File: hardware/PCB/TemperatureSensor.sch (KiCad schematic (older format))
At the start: 18 parts, among them IC1 BQ24092DGQR, IC2 ESP32-D0WD-V3, IC3 SHT31-ARP-B2.5kS, J1 USB_B_Micro, U1 LTR-329ALS-01, U2 FT230XQ

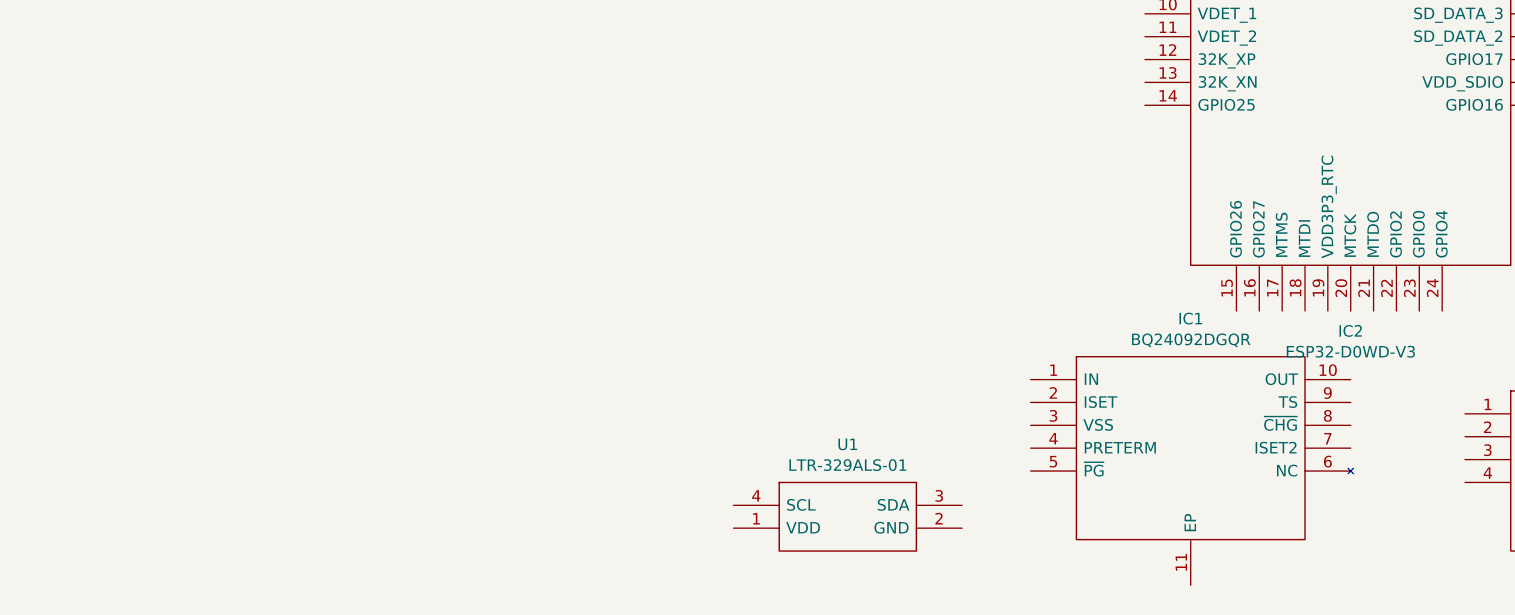
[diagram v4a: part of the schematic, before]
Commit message: Add BQ24092DGQR for LiPo charging
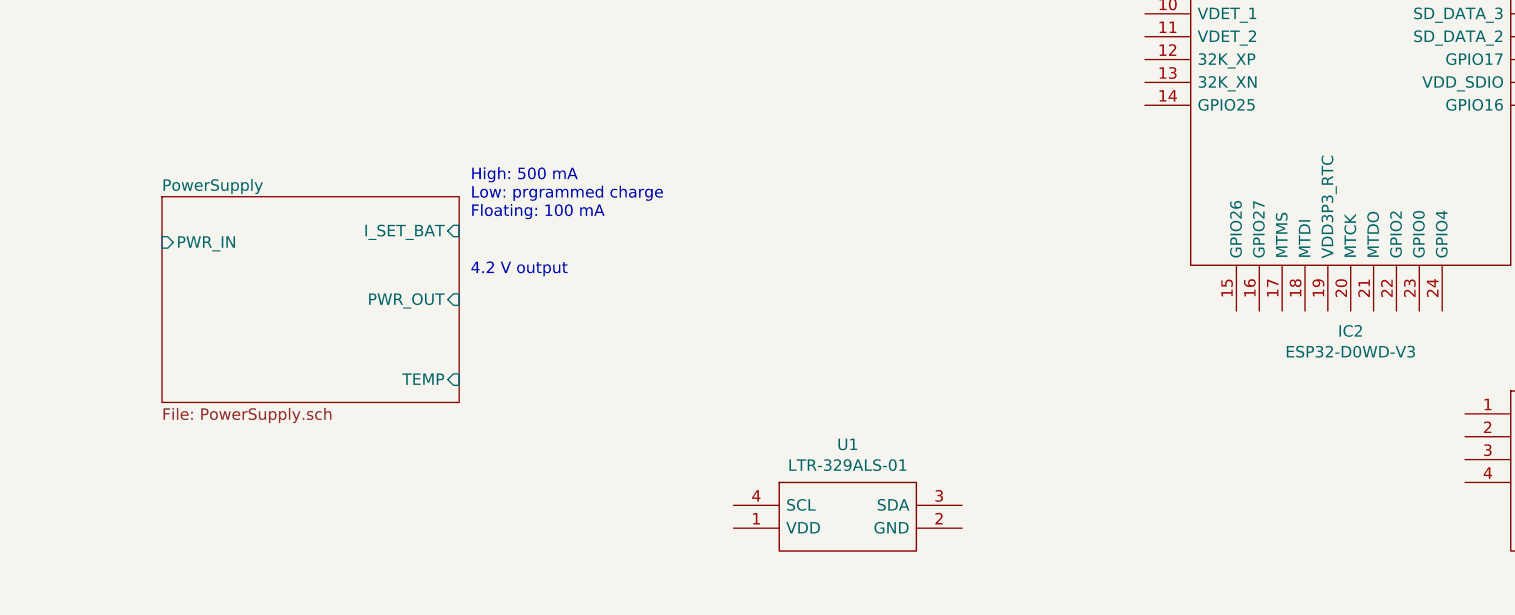
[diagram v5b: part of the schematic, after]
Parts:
- removed IC1: BQ24092DGQR, SOP50P490X110-11N, symbol ProjectLibrary:BQ24092DGQR
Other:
- note added: "4.2 V output"
- note added: "High: 500 mA\nLow: prgrammed charge\nFloating: 100 mA"
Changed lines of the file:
@@
 $Descr A4 11693 8268
 encoding utf-8
-Sheet 1 2
+Sheet 1 3
 Title ""
 Date ""
@@
 Comment4 ""
 $EndDescr
-$Comp
-L ProjectLibrary:BQ24092DGQR IC1
-U 1 1 5FB42655
-P 7900 5500
-F 0 "IC1" H 8600 5765 50  0000 C CNN
-F 1 "BQ24092DGQR" H 8600 5674 50  0000 C CNN
-F 2 "SOP50P490X110-11N" H 9150 5600 50  0001 L CNN
-F 3 "http://www.ti.com/lit/gpn/BQ24092" H 9150 5500 50  0001 L CNN
-F 4 "1A, Single-Input, Single-Cell Li-Ion Battery Charger with Operation Over JEITA and 10k NTC" H 9150 5400 50  0001 L CNN "Description"
-F 5 "1.1" H 9150 5300 50  0001 L CNN "Height"
-F 6 "595-BQ24092DGQR" H 9150 5200 50  0001 L CNN "Mouser Part Number"
-F 7 "https://www.mouser.co.uk/ProductDetail/Texas-Instruments/BQ24092DGQR?qs=C44r%252BX3hXgKGrpCEuObqhg%3D%3D" H 9150 5100 50  0001 L CNN "Mouser Price/Stock"
-F 8 "Texas Instruments" H 9150 5000 50  0001 L CNN "Manufacturer_Name"
-F 9 "BQ24092DGQR" H 9150 4900 50  0001 L CNN "Manufacturer_Part_Number"
-	1    7900 5500
-	1    0    0    -1
-$EndComp
 $Comp
 L ProjectLibrary:ESP32-D0WD-V3 IC2
@@
 Wire Wire Line
 	600  2950 600  3150
+$Sheet
+S 4100 4700 1300 900
+U 5FBFD530
+F0 "PowerSupply" 50
+F1 "PowerSupply.sch" 50
+F2 "PWR_IN" I L 4100 4900 50
+F3 "I_SET_BAT" I R 5400 4850 50
+F4 "TEMP" I R 5400 5500 50
+F5 "PWR_OUT" I R 5400 5150 50
+$EndSheet
+Text Notes 5450 4800 0    50   ~ 0
+High: 500 mA\nLow: prgrammed charge\nFloating: 100 mA
+Text Notes 5450 5050 0    50   ~ 0
+4.2 V output
 $EndSCHEMATC

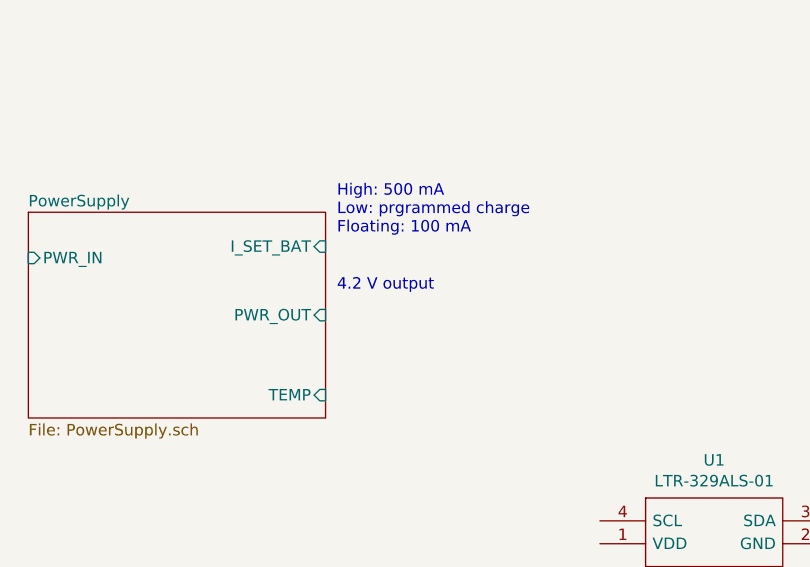
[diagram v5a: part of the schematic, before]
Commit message: Add TPS62290DRV to PowerSupply
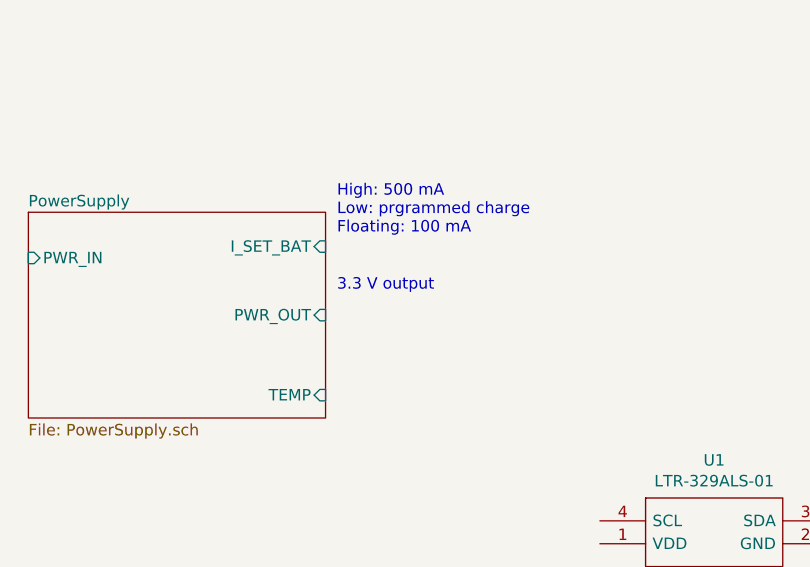
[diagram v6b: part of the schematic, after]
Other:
- note added: "3.3 V output"
- note removed: "4.2 V output"
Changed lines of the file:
@@
 High: 500 mA\nLow: prgrammed charge\nFloating: 100 mA
 Text Notes 5450 5050 0    50   ~ 0
-4.2 V output
+3.3 V output
 $EndSCHEMATC

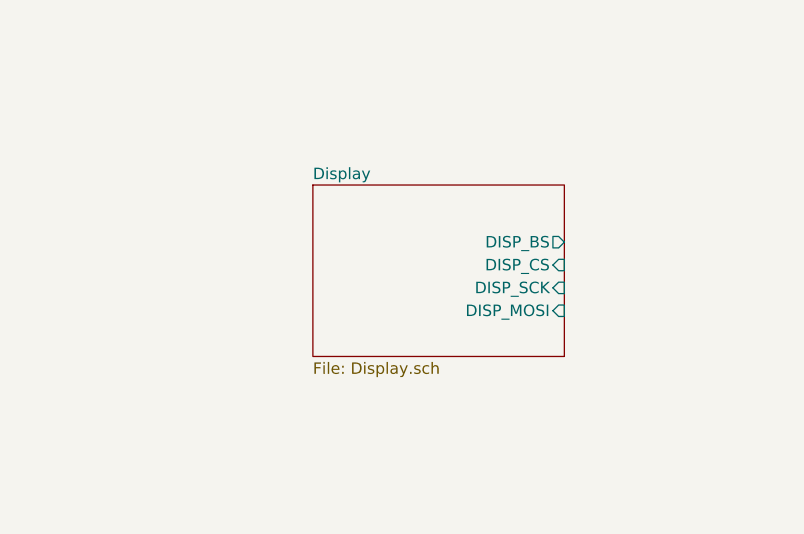
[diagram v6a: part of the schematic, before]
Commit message: complete display circuit
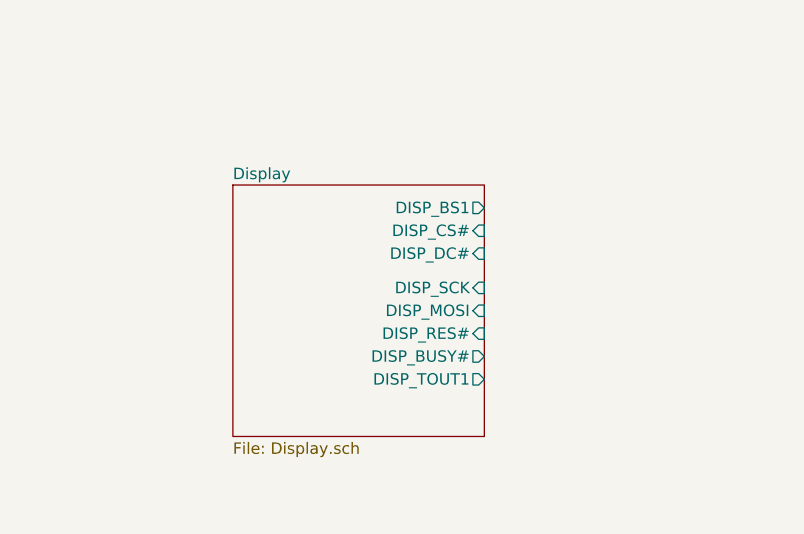
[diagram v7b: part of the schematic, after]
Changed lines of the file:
@@
 Wire Wire Line
 	5850 1500 5850 1400
-$Sheet
-S 1800 5000 1100 750
-U 5FC321F3
-F0 "Display" 50
-F1 "Display.sch" 50
-F2 "DISP_BS" O R 2900 5250 50
-F3 "DISP_CS" I R 2900 5350 50
-F4 "DISP_SCK" I R 2900 5450 50
-F5 "DISP_MOSI" I R 2900 5550 50
-$EndSheet
 $Comp
 L Mechanical:MountingHole_Pad H1
@@
 	900  2950 600  2950
 $Comp
-L power:GND #PWR?
+L power:GND #PWR01
 U 1 1 5FBF5B51
 P 600 3150
-F 0 "#PWR?" H 600 2900 50  0001 C CNN
+F 0 "#PWR01" H 600 2900 50  0001 C CNN
 F 1 "GND" H 605 2977 50  0000 C CNN
 F 2 "" H 600 3150 50  0001 C CNN
@@
 Text Notes 5450 5050 0    50   ~ 0
 3.3 V output
+$Sheet
+S 1450 5000 1100 1100
+U 5FC321F3
+F0 "Display" 50
+F1 "Display.sch" 50
+F2 "DISP_SCK" I R 2550 5450 50
+F3 "DISP_MOSI" I R 2550 5550 50
+F4 "DISP_BS1" O R 2550 5100 50
+F5 "DISP_CS#" I R 2550 5200 50
+F6 "DISP_DC#" I R 2550 5300 50
+F7 "DISP_RES#" I R 2550 5650 50
+F8 "DISP_BUSY#" O R 2550 5750 50
+F9 "DISP_TOUT1" O R 2550 5850 50
+$EndSheet
 $EndSCHEMATC

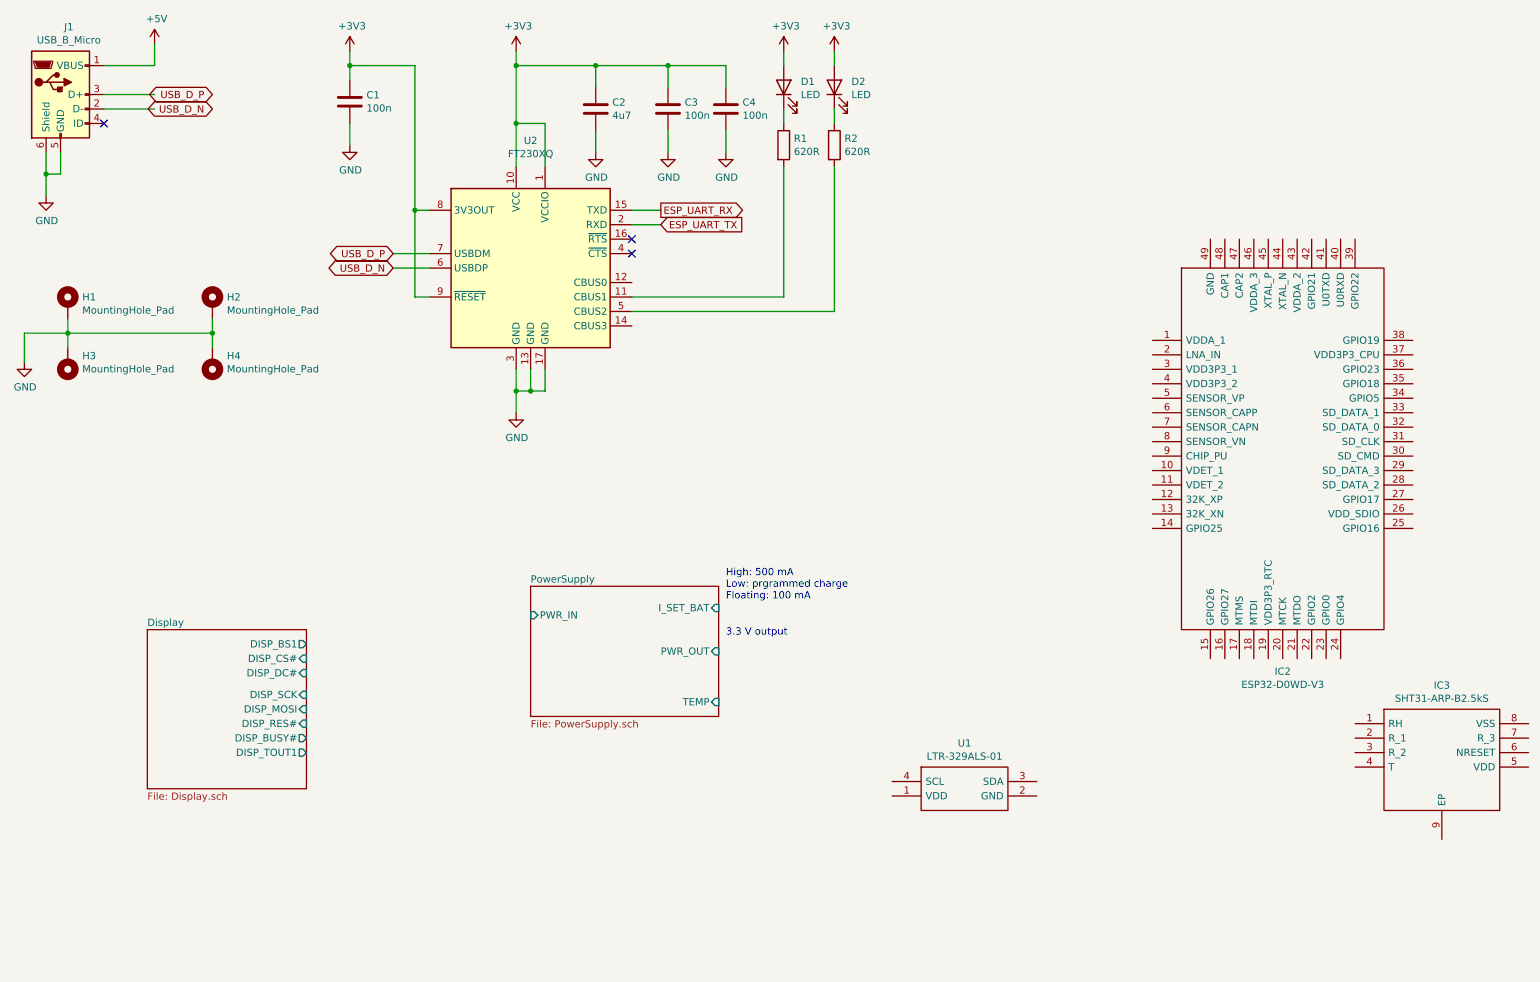
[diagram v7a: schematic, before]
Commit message: add ESP32 and Sensor Sheet
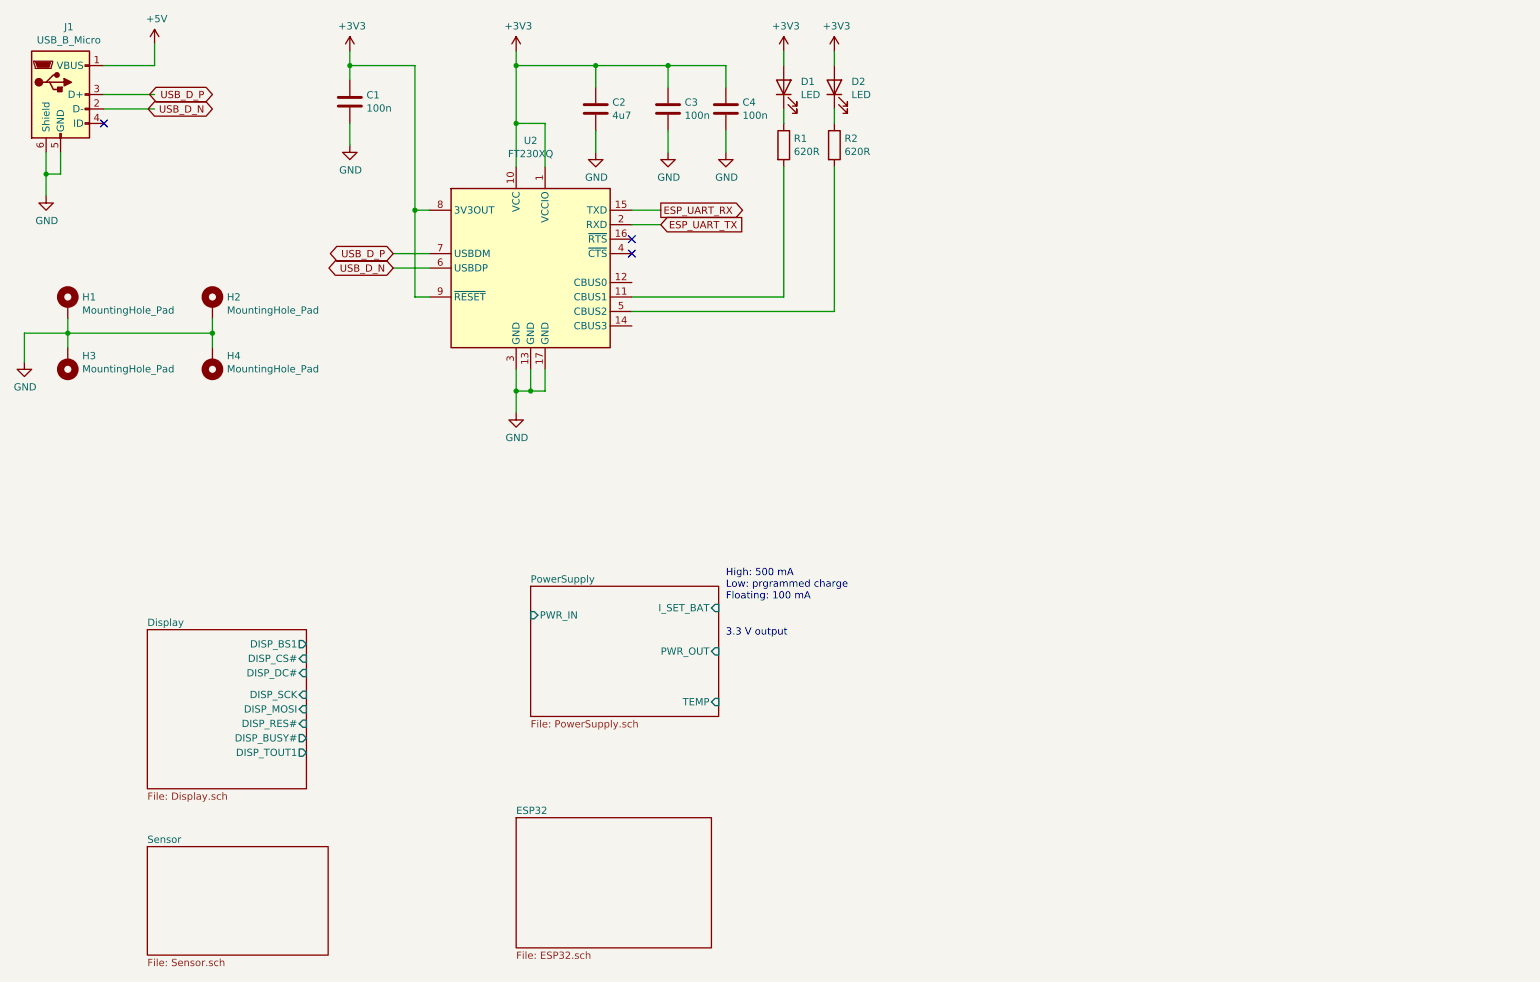
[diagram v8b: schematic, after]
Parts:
- removed IC2: ESP32-D0WD-V3, QFN35P500X500X90-49N-D, symbol ProjectLibrary:ESP32-D0WD-V3
- removed IC3: SHT31-ARP-B2.5kS, SON50P250X250X100-9N-D, symbol ProjectLibrary:SHT31-ARP-B2.5kS
- removed U1: LTR-329ALS-01, LTR329ALS01, symbol ProjectLibrary:LTR-329ALS-01
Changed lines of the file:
@@
 $Descr A4 11693 8268
 encoding utf-8
-Sheet 1 3
+Sheet 1 5
 Title ""
 Date ""
@@
 Comment4 ""
 $EndDescr
-$Comp
-L ProjectLibrary:ESP32-D0WD-V3 IC2
-U 1 1 5FB42486
-P 8400 3000
-F 0 "IC2" H 9300 711 50  0000 C CNN
-F 1 "ESP32-D0WD-V3" H 9300 620 50  0000 C CNN
-F 2 "QFN35P500X500X90-49N-D" H 10050 3500 50  0001 L CNN
-F 3 "https://www.espressif.com/sites/default/files/documentation/esp32_datasheet_en.pdf" H 10050 3400 50  0001 L CNN
-F 4 "WiFi Development Tools (802.11) SMD IC WiFi Dual Core BT Combo" H 10050 3300 50  0001 L CNN "Description"
-F 5 "0.9" H 10050 3200 50  0001 L CNN "Height"
-F 6 "356-ESP32-D0WD-V3" H 10050 3100 50  0001 L CNN "Mouser Part Number"
-F 7 "https://www.mouser.co.uk/ProductDetail/Espressif-Systems/ESP32-D0WD-V3?qs=GBLSl2AkirsI7kXw8ZPing%3D%3D" H 10050 3000 50  0001 L CNN "Mouser Price/Stock"
-F 8 "Espressif Systems" H 10050 2900 50  0001 L CNN "Manufacturer_Name"
-F 9 "ESP32-D0WD-V3" H 10050 2800 50  0001 L CNN "Manufacturer_Part_Number"
-	1    8400 3000
-	1    0    0    -1
-$EndComp
-$Comp
-L ProjectLibrary:SHT31-ARP-B2.5kS IC3
-U 1 1 5FBA3C37
-P 9800 5650
-F 0 "IC3" H 10400 5915 50  0000 C CNN
-F 1 "SHT31-ARP-B2.5kS" H 10400 5824 50  0000 C CNN
-F 2 "SON50P250X250X100-9N-D" H 10850 5750 50  0001 L CNN
-F 3 "https://componentsearchengine.com/Datasheets/1/SHT31-ARP-B2.5kS.pdf" H 10850 5650 50  0001 L CNN
-F 4 "Board Mount Humidity Sensors +/- 2%RH 14 bit Resolution" H 10850 5550 50  0001 L CNN "Description"
-F 5 "1" H 10850 5450 50  0001 L CNN "Height"
-F 6 "403-SHT31-ARP-B" H 10850 5350 50  0001 L CNN "Mouser Part Number"
-F 7 "https://www.mouser.co.uk/ProductDetail/Sensirion/SHT31-ARP-B25kS?qs=y6ZabgHbY%252BxqV2K0yYcGiA%3D%3D" H 10850 5250 50  0001 L CNN "Mouser Price/Stock"
-F 8 "Sensirion" H 10850 5150 50  0001 L CNN "Manufacturer_Name"
-F 9 "SHT31-ARP-B2.5kS" H 10850 5050 50  0001 L CNN "Manufacturer_Part_Number"
-	1    9800 5650
-	1    0    0    -1
-$EndComp
-$Comp
-L ProjectLibrary:LTR-329ALS-01 U1
-U 1 1 5FBA3CE3
-P 6600 6050
-F 0 "U1" H 7100 6315 50  0000 C CNN
-F 1 "LTR-329ALS-01" H 7100 6224 50  0000 C CNN
-F 2 "LTR329ALS01" H 7450 6150 50  0001 L CNN
-F 3 "" H 7450 6050 50  0001 L CNN
-F 4 "Ambient Light Sensors Ambient Light Photo Sensor" H 7450 5950 50  0001 L CNN "Description"
-F 5 "0" H 7450 5850 50  0001 L CNN "Height"
-F 6 "859-LTR-329ALS-01" H 7450 5750 50  0001 L CNN "Mouser Part Number"
-F 7 "https://www.mouser.co.uk/ProductDetail/Lite-On/LTR-329ALS-01?qs=Ml%2FaxAEbwm8eHg8LIDPUrw%3D%3D" H 7450 5650 50  0001 L CNN "Mouser Price/Stock"
-F 8 "Lite-On" H 7450 5550 50  0001 L CNN "Manufacturer_Name"
-F 9 "LTR-329ALS-01" H 7450 5450 50  0001 L CNN "Manufacturer_Part_Number"
-	1    6600 6050
-	1    0    0    -1
-$EndComp
 $Comp
 L Connector:USB_B_Micro J1
@@
 F9 "DISP_TOUT1" O R 2550 5850 50
 $EndSheet
+$Sheet
+S 1450 6500 1250 750
+U 5FCF6796
+F0 "Sensor" 50
+F1 "Sensor.sch" 50
+$EndSheet
+$Sheet
+S 4000 6300 1350 900
+U 5FCFD0E2
+F0 "ESP32" 50
+F1 "ESP32.sch" 50
+$EndSheet
 $EndSCHEMATC
